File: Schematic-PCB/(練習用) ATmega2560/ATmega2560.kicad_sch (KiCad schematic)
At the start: 29 parts, among them J1 Conn_01x20_Pin, J2 Conn_01x06_Pin, J3 Conn_01x06_Pin, J4 Conn_01x26_Pin, SW1 SW_Push, SW2 SW_Push, SW3 SW_Push, SW4 SW_Push, SW6 SW_SPDT, U1 MEGA_PRO_EMBED_CH340G___ATMEG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

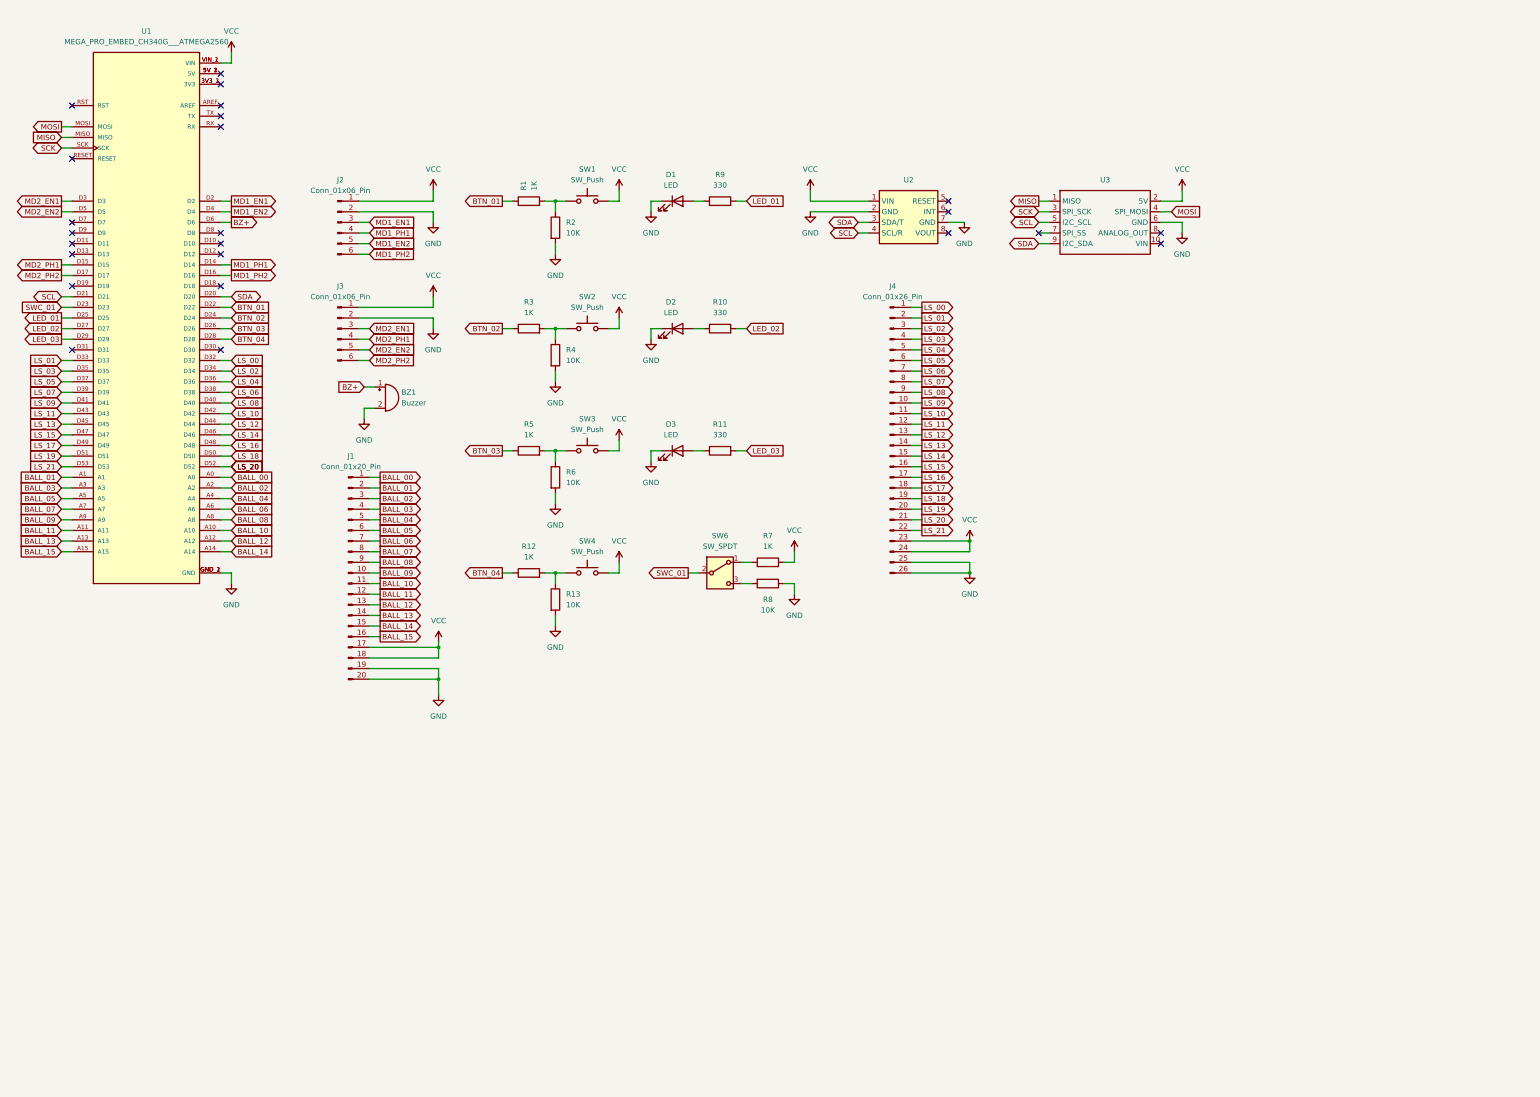
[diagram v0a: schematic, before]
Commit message: 回路図を更新しました
2023バージョンを参考に回路図を更新しました
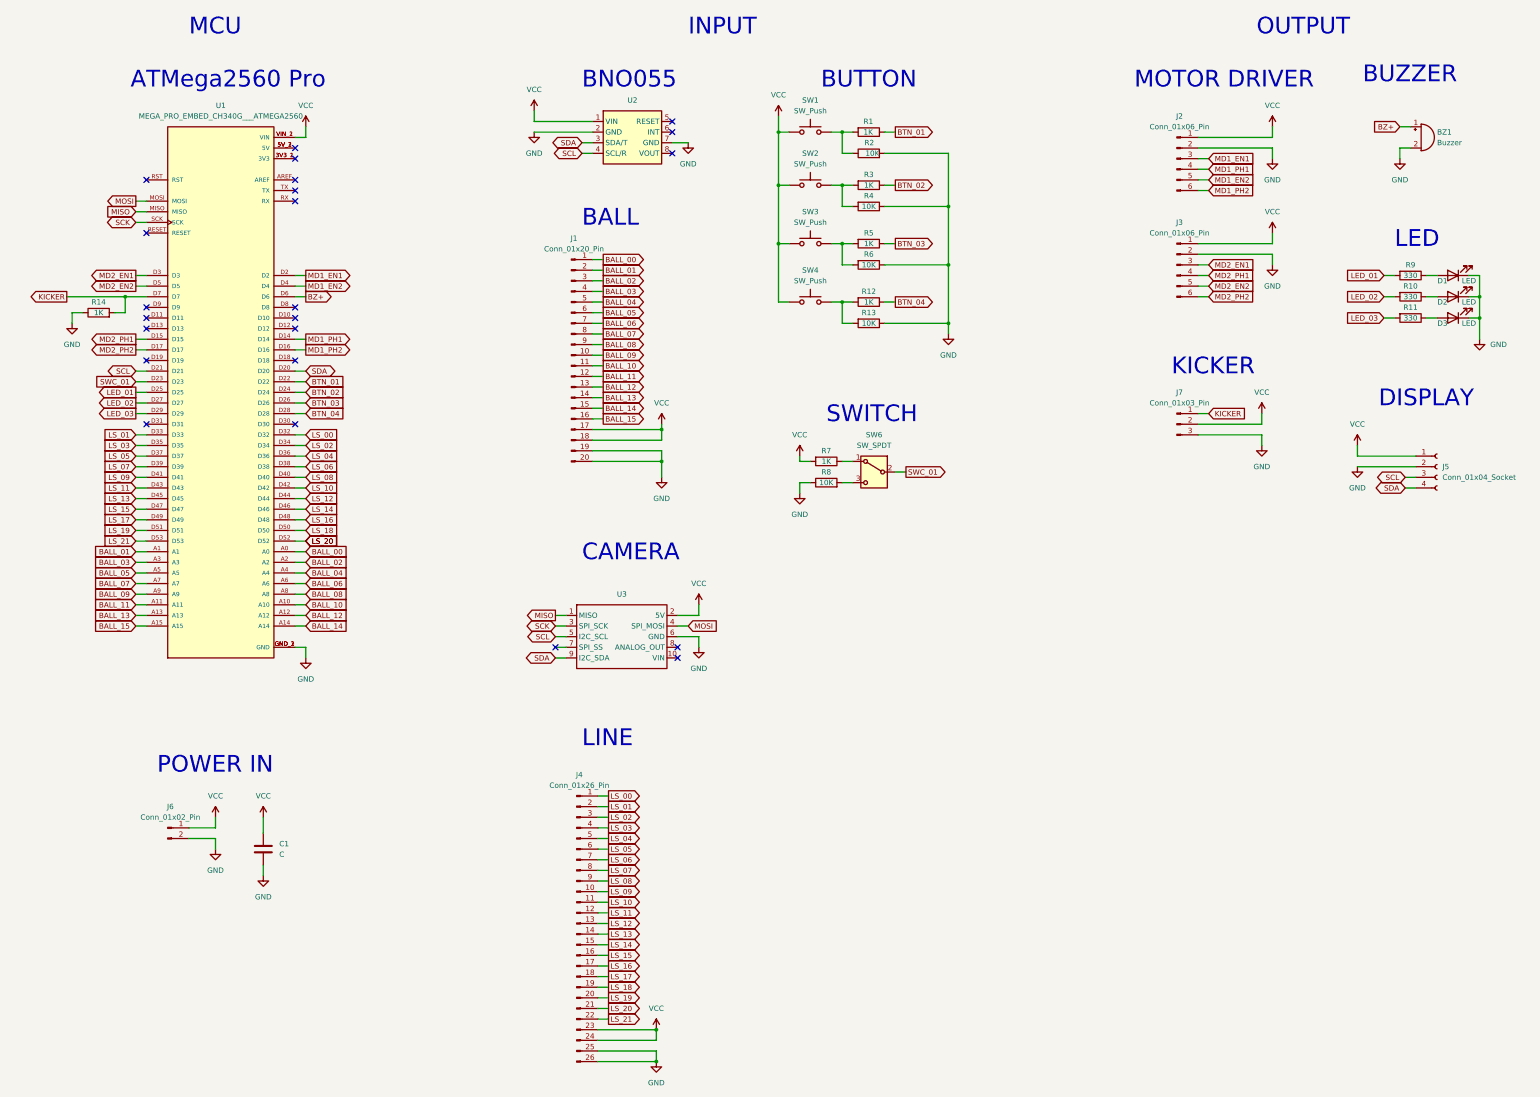
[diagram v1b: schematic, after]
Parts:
- added C1: C, symbol Device:C
- added J5: Conn_01x04_Socket, symbol Connector:Conn_01x04_Socket
- added J6: Conn_01x02_Pin, symbol Connector:Conn_01x02_Pin
- added J7: Conn_01x03_Pin, symbol Connector:Conn_01x03_Pin
- added R14: 1K, symbol Device:R
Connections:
- net GND: now also R13.1, R4.1, R6.1, C1.2, J5.2 (Pin_2), J6.2 (Pin_2), J7.3 (Pin_3), R14.1; no longer R13.2, R4.2, R6.2
- net SCL: now also J5.3 (Pin_3)
- net SDA: now also J5.4 (Pin_4)
- net VCC: now also SW1.1, SW2.1, SW3.1, SW4.1, C1.1, J5.1 (Pin_1), J6.1 (Pin_1), J7.2 (Pin_2); no longer SW1.2, SW2.2, SW3.2, SW4.2
- net at R1.2, R2.1: now also SW1.2; no longer SW1.1
- net KICKER: now reaches U1.D7
- net KICKER: now also J7.1 (Pin_1), R14.2
- new net: R5.2, R6.2, SW3.2
- new net: R3.2, R4.2, SW2.2
- new net: R12.2, R13.2, SW4.2
- no-connect marks 24 -> 23
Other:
- note added: "ATMega2560 Pro"
- note added: "BALL"
- note added: "BNO055"
- note added: "BUTTON"
- note added: "BUZZER"
- note added: "CAMERA"
- note added: "DISPLAY"
- note added: "INPUT"
- note added: "KICKER"
- note added: "LED"
- note added: "LINE"
- note added: "MCU"
- note added: "MOTOR DRIVER"
- note added: "OUTPUT"
- note added: "POWER IN"
- note added: "SWITCH"
- moved on the sheet: BZ1, D1, D2, D3, J1, J2, J3, J4, R1, R10, R11, R12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

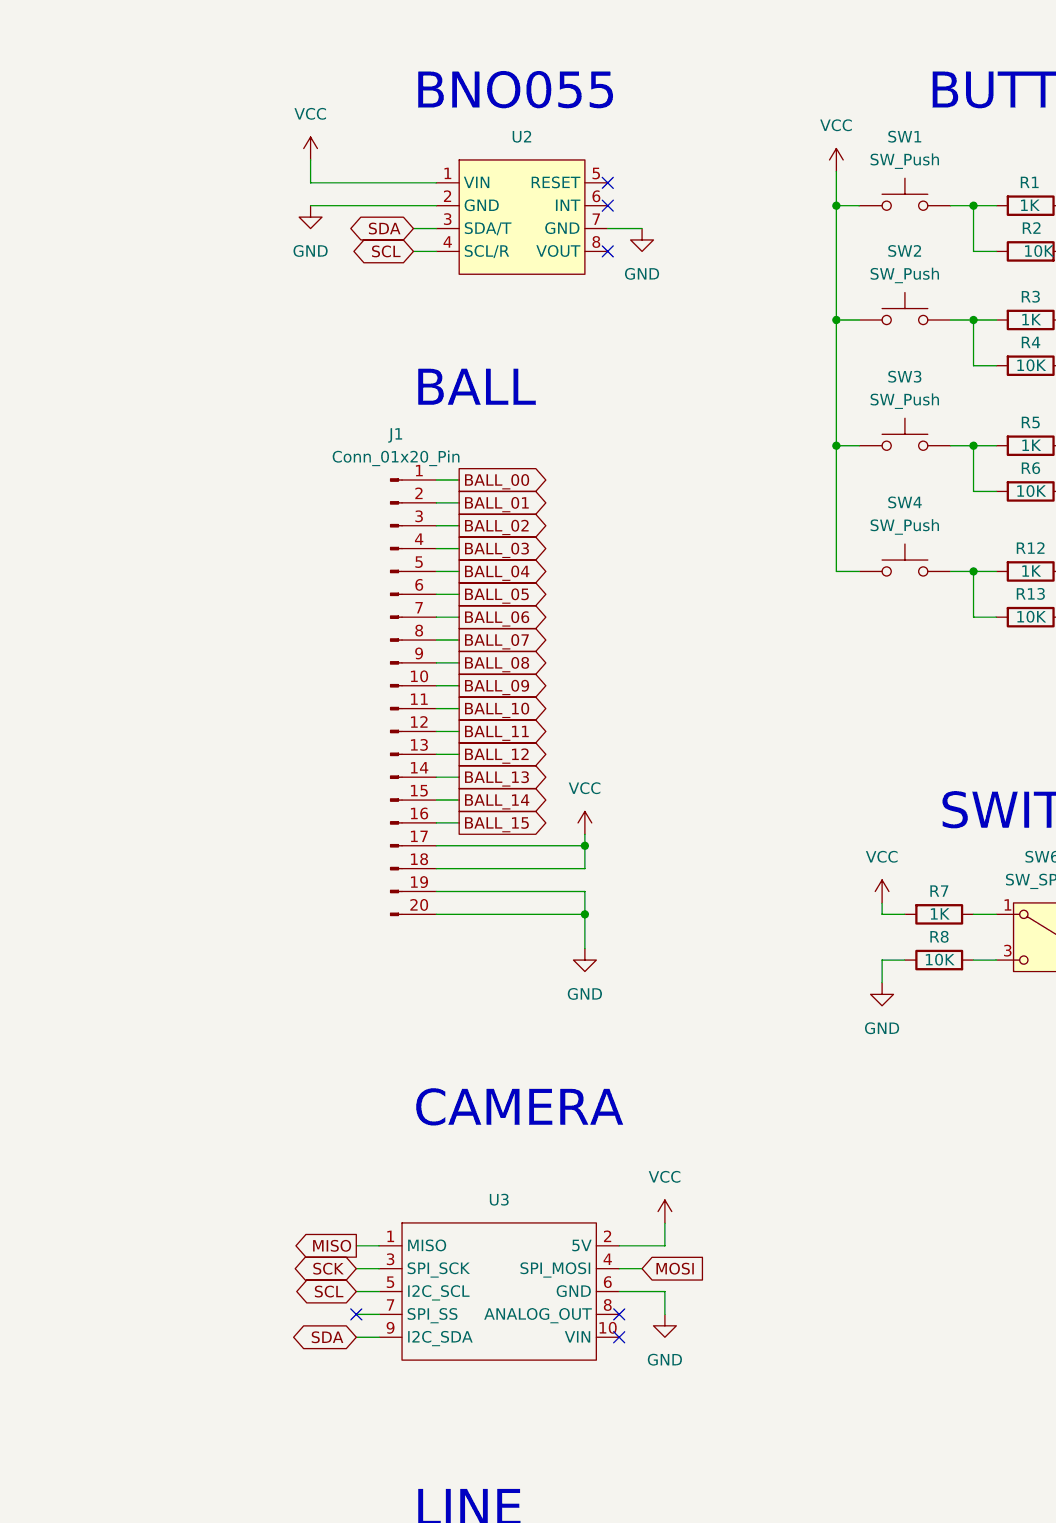
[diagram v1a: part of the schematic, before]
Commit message: (練習用)ATMega2560のPCBを編集
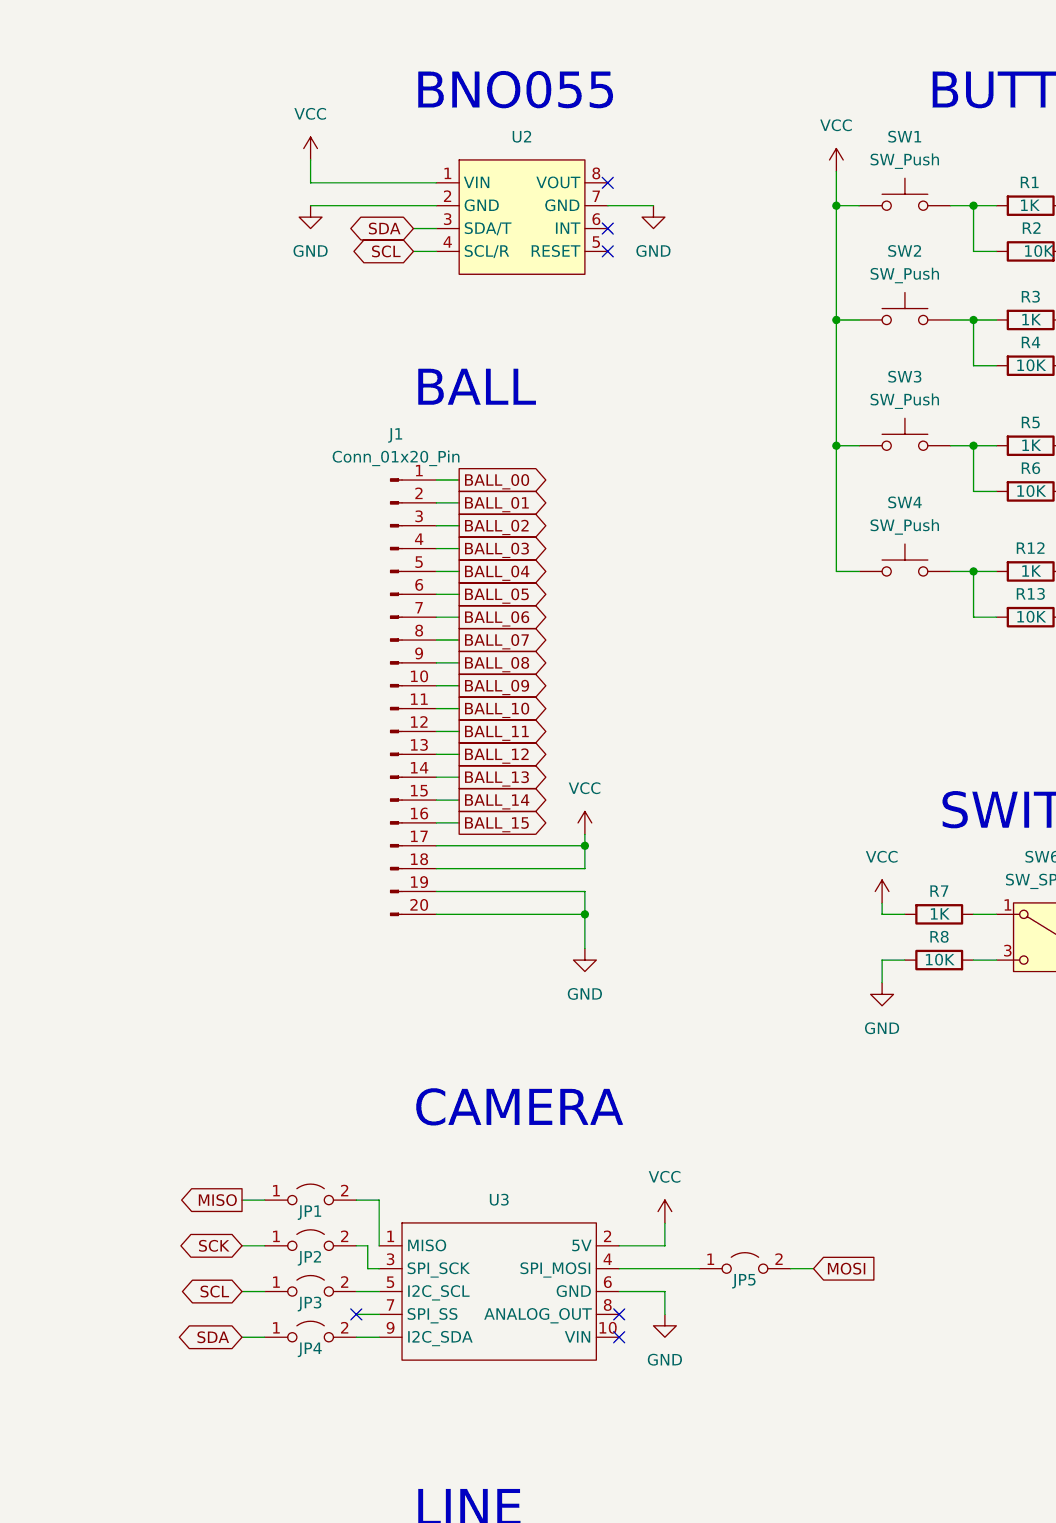
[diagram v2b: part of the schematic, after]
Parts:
- added JP1, JP2, JP3, JP4, JP5: Jumper_2_Open, Jumper:SolderJumper-2_P1.3mm_Open_Pad1.0x1.5mm, symbol Jumper:Jumper_2_Open
- BZ1: footprint (none) -> @MyLibrary:PKM13EPYH4000-A0
- C1: footprint (none) -> Capacitor_SMD:C_0805_2012Metric
- D1, D2, D3: footprint (none) -> LED_SMD:LED_0603_1608Metric
- J1: footprint (none) -> Connector_IDC:IDC-Header_2x10_P2.54mm_Vertical
- J2, J3: footprint (none) -> Connector_JST:JST_XH_B6B-XH-A_1x06_P2.50mm_Vertical
- J4: footprint (none) -> Connector_IDC:IDC-Header_2x13_P2.54mm_Vertical
- J5: footprint (none) -> Connector_PinSocket_2.54mm:PinSocket_1x04_P2.54mm_Vertical
- J6: footprint (none) -> Connector_JST:JST_XH_S2B-XH-A-1_1x02_P2.50mm_Horizontal
- J7: footprint (none) -> Connector_JST:JST_XH_S3B-XH-A-1_1x03_P2.50mm_Horizontal
- R1, R10, R11, R12, R13, R14, R2, R3, R4, R5, R6, R7, R8, R9: footprint (none) -> Resistor_SMD:R_0805_2012Metric
- SW1, SW2, SW3, SW4: footprint (none) -> @MyLibrary:TVBP06-BN043CB-B
- SW6: footprint (none) -> @MyLibrary:SS12D01G4-G_2
- U1: footprint MEGA_PRO_EMBED_CH340G___ATMEGA2560:MODULE_MEGA_PRO_EMBED_CH340G___ATMEGA2560 -> ATMega2560:ATMega2560
- U2: footprint (none) -> @MyLibrary:BNO055
- U3: footprint (none) -> Connector_IDC:IDC-Header_2x05_P2.54mm_Vertical
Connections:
- net MISO: now also JP1.1 (A); no longer U3.1 (MISO)
- net MOSI: now also JP5.2 (B); no longer U3.4 (SPI_MOSI)
- net SCK: now also JP2.1 (A); no longer U3.3 (SPI_SCK)
- net SCL: now also JP3.1 (A); no longer U3.5 (I2C_SCL)
- net SDA: now also JP4.1 (A); no longer U3.9 (I2C_SDA)
- new net: JP4.2 (B), U3.9 (I2C_SDA)
- new net: JP2.2 (B), U3.3 (SPI_SCK)
- new net: JP3.2 (B), U3.5 (I2C_SCL)
- new net: JP5.1 (A), U3.4 (SPI_MOSI)
- new net: JP1.2 (B), U3.1 (MISO)
